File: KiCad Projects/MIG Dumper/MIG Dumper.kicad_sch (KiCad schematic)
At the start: 17 parts, among them J1 USB_C_Receptacle_USB2.0_16P, J2 Conn_02x04_Counter_Clockwise, J3 Conn_01x17_MountingPin, U1 ESP32-S2, U2 ICE40UP5K-SG48ITR, U3 GL823K-HCY04, Y1 ECS-400-10-37B2-CKY-TR

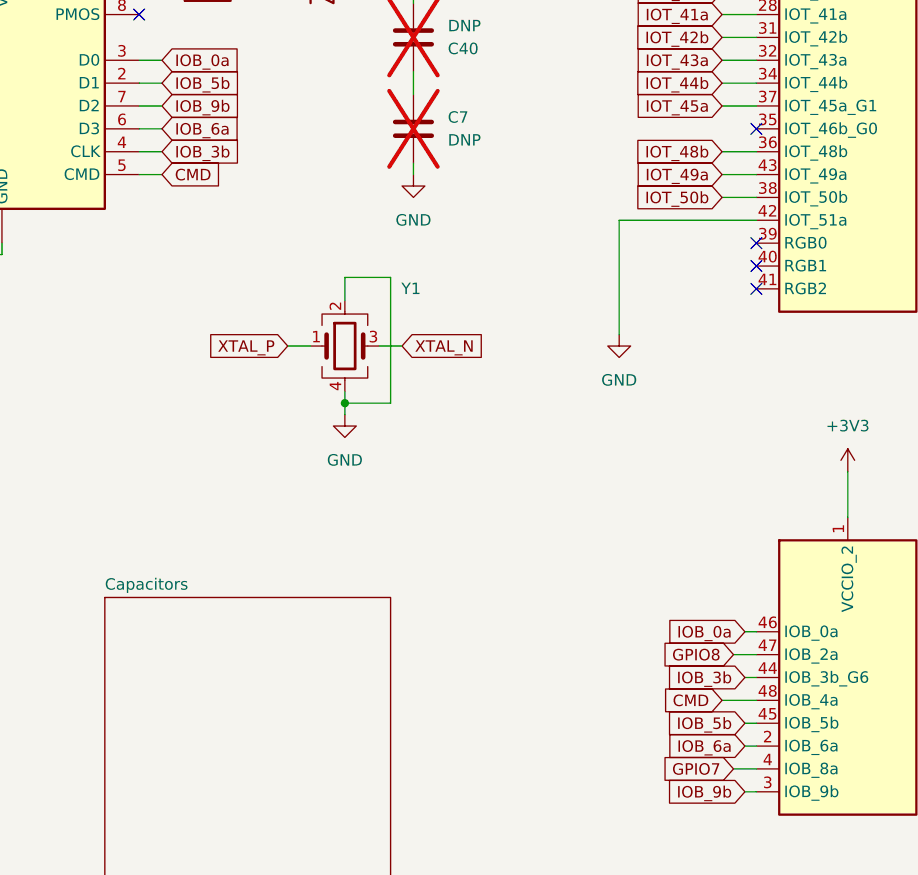
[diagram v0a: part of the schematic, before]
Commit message: Updated Flashcart PCB, uploaded Flashcart BOM
Revised the Flashcart PCB to the newer revision of the MIG v2, as well as added DigiKey and Mouser BOMs for the Flashcart. One capacitor measurement on the Dumper PCB was corrected as well.
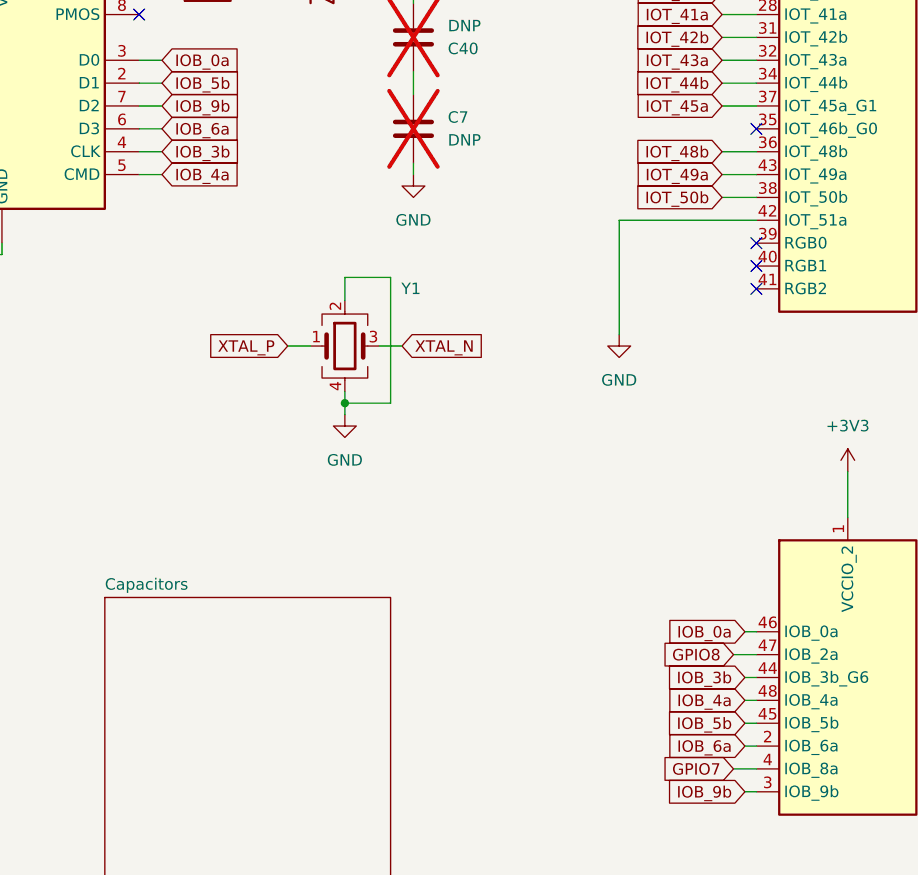
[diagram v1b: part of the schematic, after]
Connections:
- net CMD renamed IOB_4a
